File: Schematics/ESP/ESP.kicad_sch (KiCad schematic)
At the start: 29 parts, among them J1 Barrel_Jack, Q5 IRLB8721PBF, Q6 IRLB8721PBF, U1 BQ7791500PWT

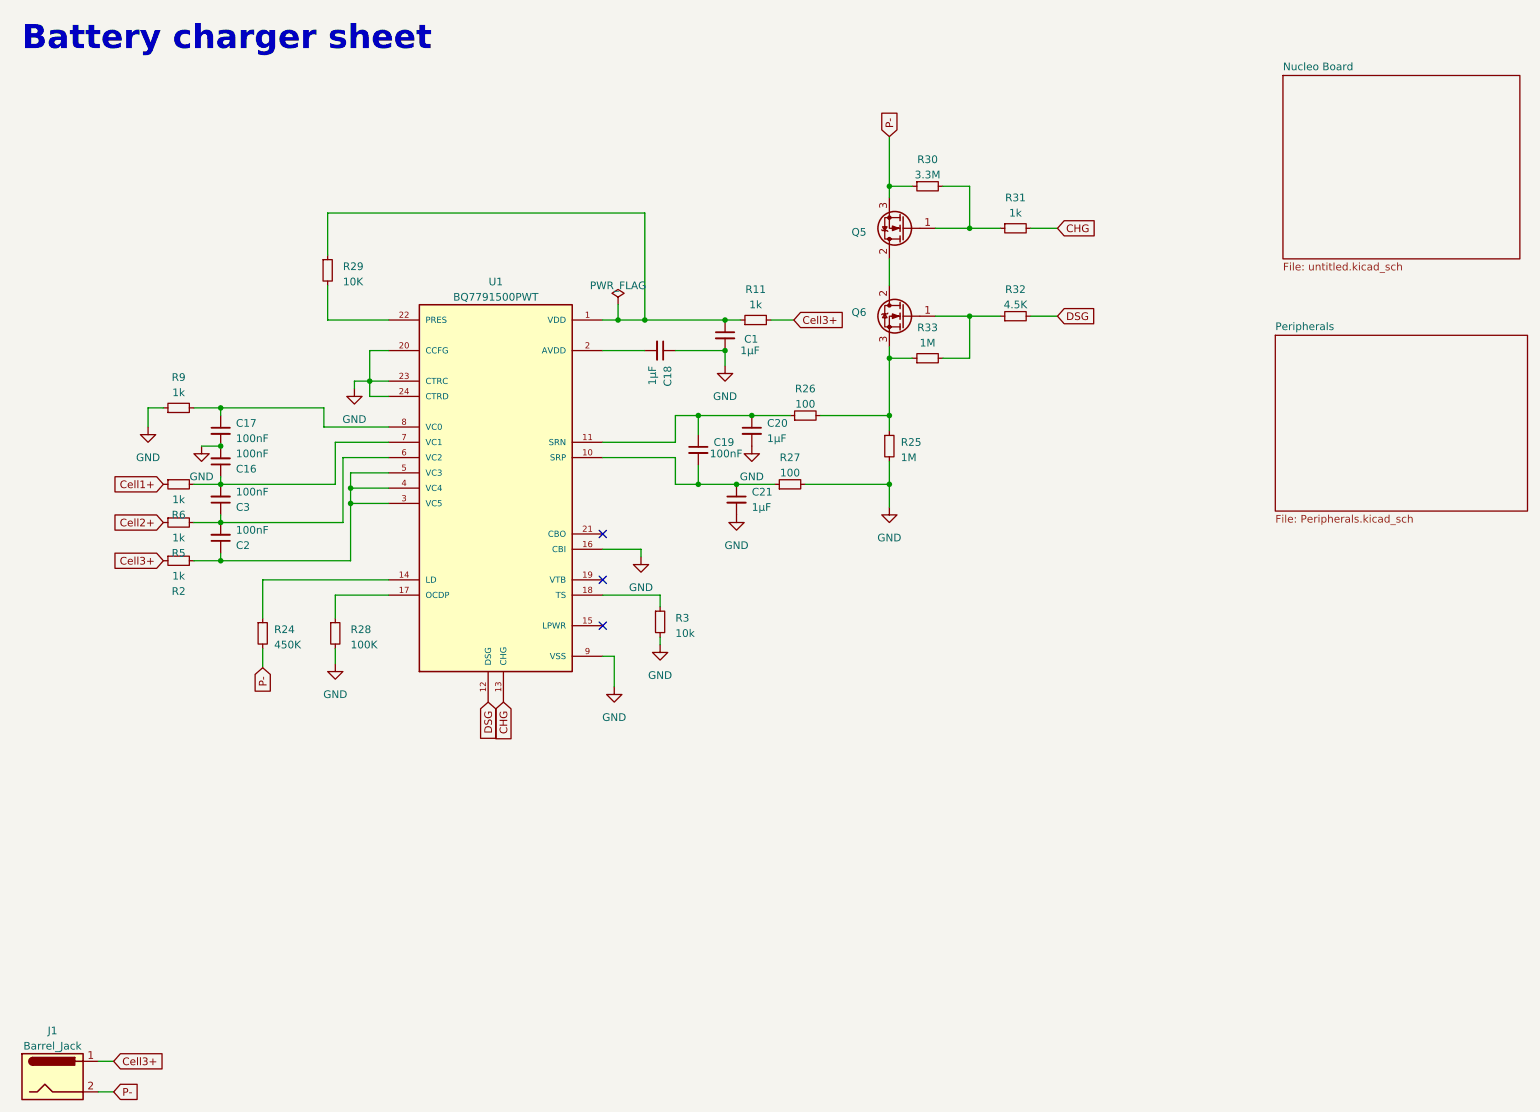
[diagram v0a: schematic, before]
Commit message: charging IC PCB and cleanup
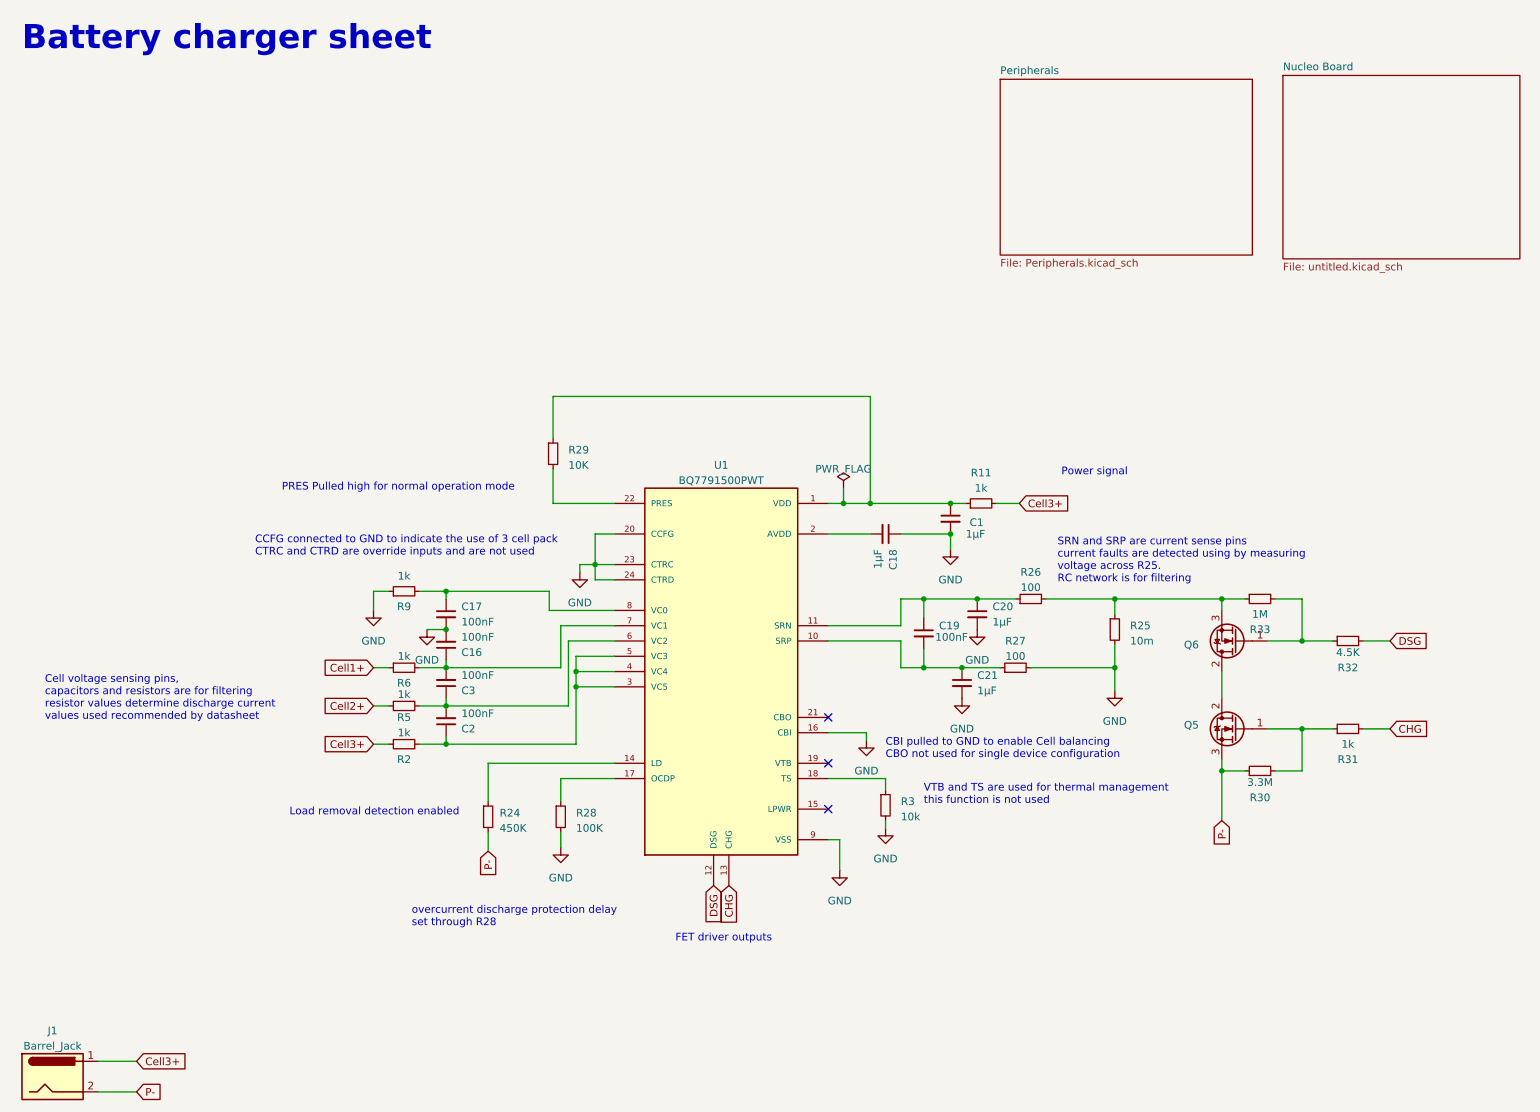
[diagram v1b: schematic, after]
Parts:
- J1: footprint RAPC722X:SWITCHCRAFT_RAPC722X -> Connector_BarrelJack:BarrelJack_GCT_DCJ200-10-A_Horizontal
- R25: value 1M -> 10m; Price 0.11 -> 0.4216; digikey link https://www.digikey.fi/en/products/detail/yageo/RC1206JR-07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 -> https://www.digikey.fi/en/products/detail/yageo/PA1206FRE07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
- U1: footprint SOP65P640X120-24N -> Package_SO:TSSOP-24_4.4x7.8mm_P0.65mm
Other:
- note added: "CBI pulled to GND to enable Cell balancing CBO not used for single device configuration"
- note added: "CCFG connected to GND to indicate the use of 3 cell pack CTRC and CTRD are override inputs and are not used"
- note added: "Cell voltage sensing pins, capacitors and resistors are for filtering resistor values determine discharge current values used recommended by datasheet"
- note added: "FET driver outputs"
- note added: "Load removal detection enabled"
- note added: "PRES Pulled high for normal operation mode"
- note added: "Power signal"
- note added: "SRN and SRP are current sense pins current faults are detected using by measuring voltage across R25. RC network is for filtering"
- note added: "VTB and TS are used for thermal management this function is not used"
- note added: "overcurrent discharge protection delay set through R28"
- moved on the sheet: C1, C16, C17, C18, C19, C2, C20, C21, C3, Q5, Q6, R11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

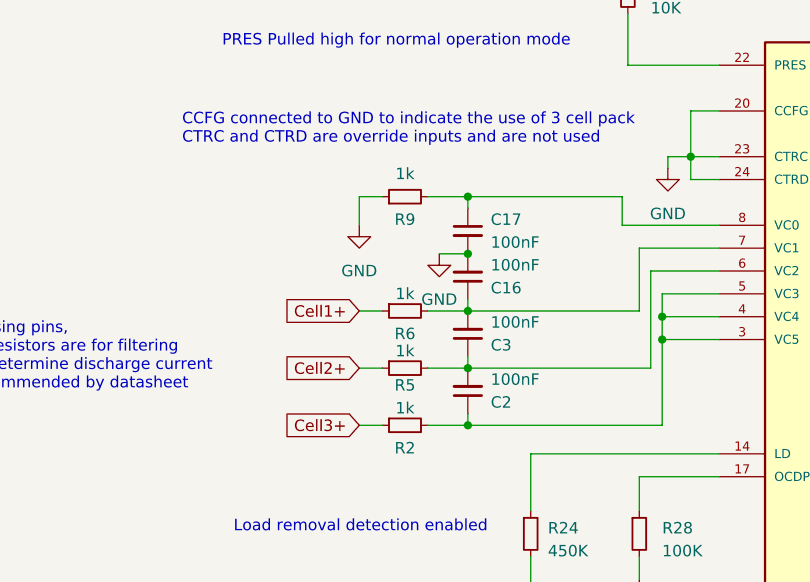
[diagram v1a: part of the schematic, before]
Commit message: fixed cell balancing speed
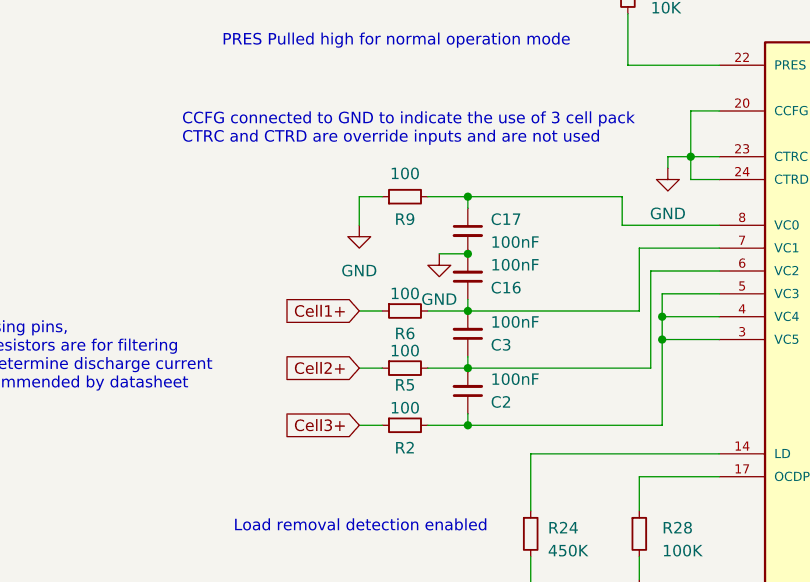
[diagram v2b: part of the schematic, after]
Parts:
- R2, R5, R6, R9: value 1k -> 100
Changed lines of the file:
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@@
       (effects (font (size 1.27 1.27)))
     )
-    (property "Value" "1k" (at 81.28 133.35 90)
+    (property "Value" "100" (at 81.28 133.35 90)
       (effects (font (size 1.27 1.27)))
     )
@@
       (effects (font (size 1.27 1.27)))
     )
-    (property "Value" "1k" (at 81.28 120.65 90)
+    (property "Value" "100" (at 81.28 120.65 90)
       (effects (font (size 1.27 1.27)))
     )
@@
       (effects (font (size 1.27 1.27)))
     )
-    (property "Value" "1k" (at 81.28 127 90)
+    (property "Value" "100" (at 81.28 127 90)
       (effects (font (size 1.27 1.27)))
     )
@@
       (effects (font (size 1.27 1.27)))
     )
-    (property "Value" "1k" (at 81.28 107.315 90)
-      (effects (font (size 1.27 1.27)))
-    )
+    (property "Value" "100" (at 81.28 107.315 90)
+      (effects (font (size 1.27 1.27)))
+    )

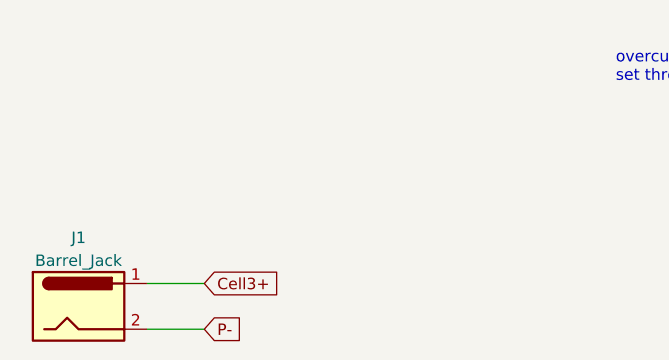
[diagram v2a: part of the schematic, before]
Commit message: fixed power tracks
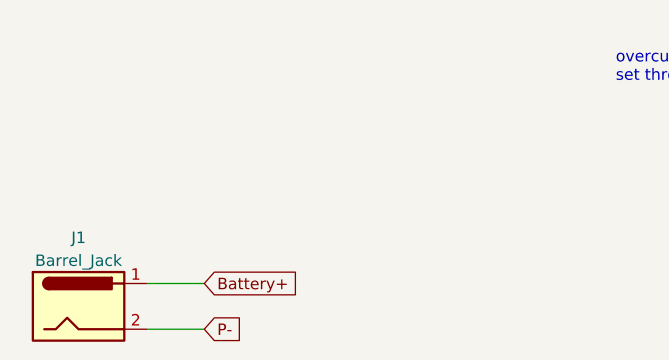
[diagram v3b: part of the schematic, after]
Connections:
- net Cell3+: no longer J1.1
- new net Battery+: J1.1
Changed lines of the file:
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@@
     )
   )
-  (global_label "Cell3+" (shape input) (at 36.83 187.96 0) (fields_autoplaced)
+  (global_label "Battery+" (shape input) (at 36.83 187.96 0) (fields_autoplaced)
     (effects (font (size 1.27 1.27)) (justify left))
-    (property "Intersheetrefs" "${INTERSHEET_REFS}" (at 46.2067 187.96 0)
+    (property "Intersheetrefs" "${INTERSHEET_REFS}" (at 48.021 187.96 0)
       (effects (font (size 1.27 1.27)) (justify left) hide)
     )
